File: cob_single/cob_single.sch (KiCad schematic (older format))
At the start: 26 parts, among them J1 Conn_01x03, J2 Conn_01x03, Q1 Q_NPN_BEC, Q2 Q_NPN_BEC, Q3 Q_NPN_BEC, U1 MOSFET_N_SI3424CDV-T1-GE3, U2 MOSFET_N_SI3424CDV-T1-GE3, U3 MOSFET_N_SI3424CDV-T1-GE3, U4 WS2811, U5 3_Inverter_TC7WH14FU,LJ(CT

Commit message: WIP rev v1.0
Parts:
- added H1, H2, H3, H4: MountingHole, homebrew:MountingHole_2.7mm_M2.5, symbol Mechanical:MountingHole
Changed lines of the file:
@@
 Wire Wire Line
 	1650 1150 1750 1150
+$Comp
+L Mechanical:MountingHole H1
+U 1 1 5DBB75AD
+P 9850 3250
+F 0 "H1" H 9950 3296 50  0000 L CNN
+F 1 "MountingHole" H 9950 3205 50  0000 L CNN
+F 2 "homebrew:MountingHole_2.7mm_M2.5" H 9850 3250 50  0001 C CNN
+F 3 "~" H 9850 3250 50  0001 C CNN
+	1    9850 3250
+	1    0    0    -1
+$EndComp
+$Comp
+L Mechanical:MountingHole H2
+U 1 1 5DBB979C
+P 9850 3400
+F 0 "H2" H 9950 3446 50  0000 L CNN
+F 1 "MountingHole" H 9950 3355 50  0000 L CNN
+F 2 "homebrew:MountingHole_2.7mm_M2.5" H 9850 3400 50  0001 C CNN
+F 3 "~" H 9850 3400 50  0001 C CNN
+	1    9850 3400
+	1    0    0    -1
+$EndComp
+$Comp
+L Mechanical:MountingHole H3
+U 1 1 5DBB99C6
+P 9850 3550
+F 0 "H3" H 9950 3596 50  0000 L CNN
+F 1 "MountingHole" H 9950 3505 50  0000 L CNN
+F 2 "homebrew:MountingHole_2.7mm_M2.5" H 9850 3550 50  0001 C CNN
+F 3 "~" H 9850 3550 50  0001 C CNN
+	1    9850 3550
+	1    0    0    -1
+$EndComp
+$Comp
+L Mechanical:MountingHole H4
+U 1 1 5DBB9B70
+P 9850 3700
+F 0 "H4" H 9950 3746 50  0000 L CNN
+F 1 "MountingHole" H 9950 3655 50  0000 L CNN
+F 2 "homebrew:MountingHole_2.7mm_M2.5" H 9850 3700 50  0001 C CNN
+F 3 "~" H 9850 3700 50  0001 C CNN
+	1    9850 3700
+	1    0    0    -1
+$EndComp
 $EndSCHEMATC

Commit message: Re-do revision 1.0 with 5V switching driver
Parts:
- removed Q1, Q2, Q3: Q_NPN_BEC, Package_TO_SOT_SMD:SOT-23, symbol Device:Q_NPN_BEC
- removed R6, R8: .36, Resistor_SMD:R_0805_2012Metric_Pad1.15x1.40mm_HandSolder, symbol Device:R
- removed R7: 100, Resistor_SMD:R_0603_1608Metric, symbol Device:R
- removed U1, U2, U3: MOSFET_N_SI3424CDV-T1-GE3, homebrew:6-TSOP-MOSFET-SI3424CDV-T1-GE3, symbol Homebrew:MOSFET_N_SI3424CDV-T1-GE3
- added C5, C6, C7, C8, C9: 10uF, Capacitor_SMD:C_0805_2012Metric, symbol Device:C
- added L1, L2, L3: 4.7uH, homebrew:1008_(2520_METRIC), symbol Device:L
- added U1, U2, U3: PAM2804_LED_DRIVER, Package_TO_SOT_SMD:TSOT-23-5, symbol Homebrew:PAM2804_LED_DRIVER
- R1, R4: value 100 -> .143
- R2: value .36 -> .143; footprint Resistor_SMD:R_0805_2012Metric_Pad1.15x1.40mm_HandSolder -> Resistor_SMD:R_0603_1608Metric
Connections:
- net labels added: B_LED_ANODE, B_LED_CATHODE, G_LED_ANODE, G_LED_CATHODE, R_LED_ANODE, R_LED_CATHODE
- net labels removed: B_LED, G_LED, R_LED
- wire segments 54 -> 59
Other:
- moved on the sheet: D1

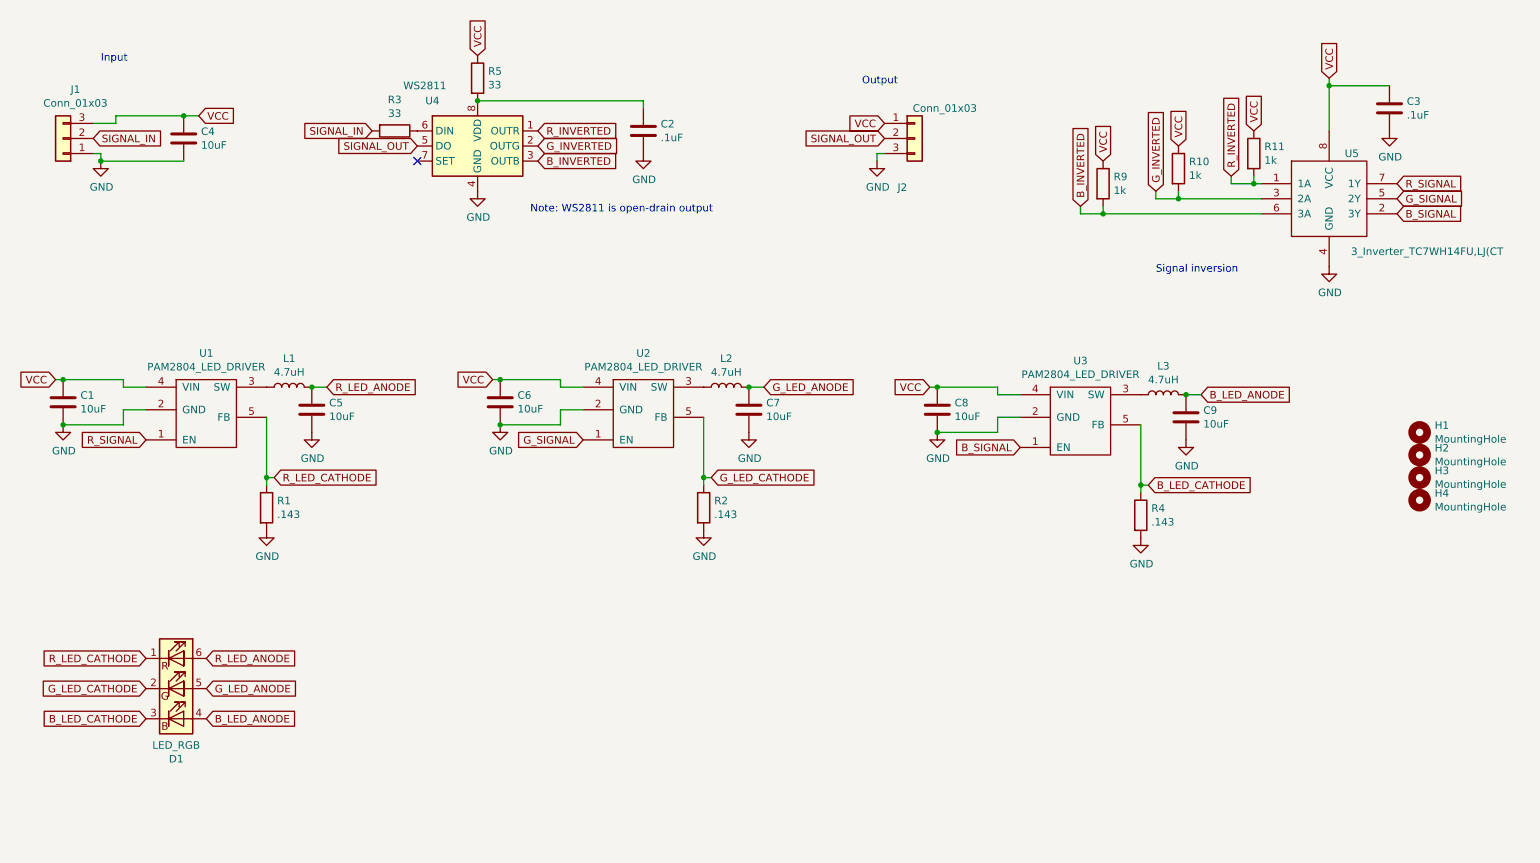
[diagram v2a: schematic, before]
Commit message: Convert v1.0 to 12v supply/12v tolerant switching driver.
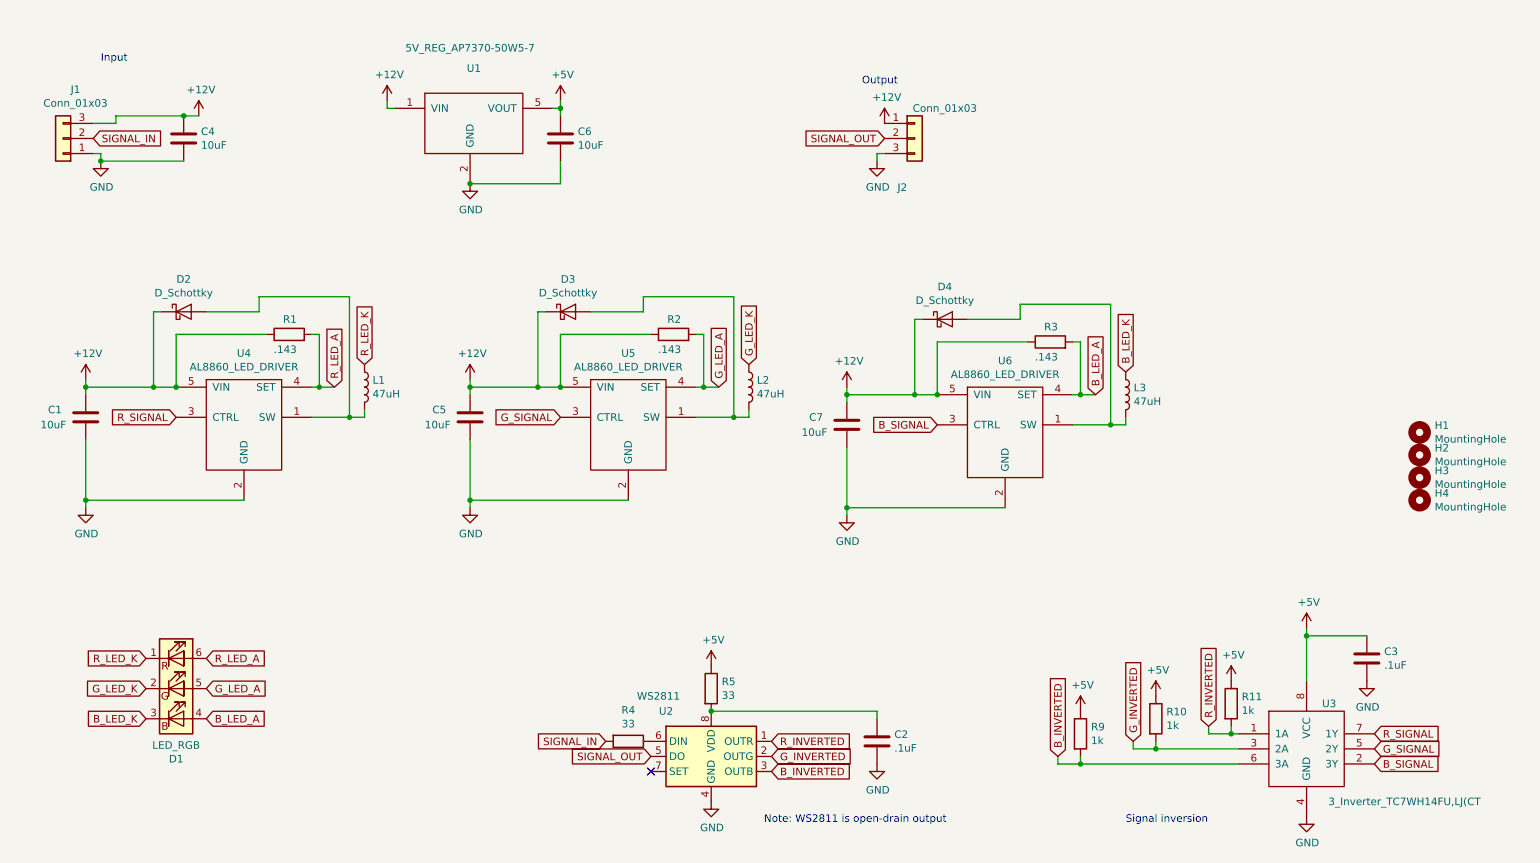
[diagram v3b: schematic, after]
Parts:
- removed C8, C9: 10uF, Capacitor_SMD:C_0805_2012Metric, symbol Device:C
- removed R4: .143, Resistor_SMD:R_0603_1608Metric, symbol Device:R
- removed U1, U2, U3: PAM2804_LED_DRIVER, Package_TO_SOT_SMD:TSOT-23-5, symbol Homebrew:PAM2804_LED_DRIVER
- added D2, D3, D4: D_Schottky, Diode_SMD:D_SOD-123F, symbol Device:D_Schottky
- added R3: .143, Resistor_SMD:R_0805_2012Metric, symbol Device:R
- added U1: 5V_REG_AP7370-50W5-7, Package_TO_SOT_SMD:TSOT-23-5, symbol Homebrew:5V_REG_AP7370-50W5-7
- added U4, U5, U6: AL8860_LED_DRIVER, homebrew:SOT-25, symbol Homebrew:AL8860_LED_DRIVER
- L1, L2, L3: value 4.7uH -> 47uH; footprint homebrew:1008_(2520_METRIC) -> Inductor_SMD:L_Taiyo-Yuden_NR-60xx
- R1, R2: footprint Resistor_SMD:R_0603_1608Metric -> Resistor_SMD:R_0805_2012Metric
- renumbered R3 to R4, U4 to U2, U5 to U3
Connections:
- net B_LED_CATHODE is gone; now on net B_LED_K: D1.3 (BK)
- net B_SIGNAL: now also U6.3 (CTRL)
- net GND: now also U1.2 (GND), U4.2 (GND), U5.2 (GND), U6.2 (GND); no longer R1.2, R2.2
- net G_SIGNAL: now also U5.3 (CTRL)
- net R_SIGNAL: now also U4.3 (CTRL)
- net R_LED_K: now reaches L1.1
- net R_LED_K: now also D1.1 (RK)
- net G_LED_K: now reaches L2.1
- net G_LED_K: now also D1.2 (GK)
- net B_LED_K: now reaches L3.1
- net B_LED_ANODE: no longer names the net of L3.2
- net B_LED_ANODE: now also D4.2 (A), U6.1 (SW); no longer D1.4 (BA)
- removed net G_LED_ANODE: C7.1, D1.5 (GA), L2.2
- net G_LED_CATHODE renamed +12V
- net +12V: now also C1.1, C4.1, C5.1, C7.1, J1.3 (Pin_3), J2.1 (Pin_1), R1.1, D2.1 (K), D3.1 (K), D4.1 (K), R3.1, U1.1 (VIN), U4.5 (VIN), U5.5 (VIN), U6.5 (VIN); no longer D1.2 (GK)
- removed net R_LED_ANODE: C5.1, D1.6 (RA), L1.2
- removed net R_LED_CATHODE: D1.1 (RK), R1.1
- net VCC renamed +5V
- net +5V: now also U1.5 (VOUT); no longer C1.1, C4.1, J1.3 (Pin_3), J2.1 (Pin_1)
- new net: D2.2 (A), L1.2, U4.1 (SW)
- new net: D3.2 (A), L2.2, U5.1 (SW)
- new net B_LED_A: D1.4 (BA), R3.2, U6.4 (SET)
- new net G_LED_A: D1.5 (GA), R2.2, U5.4 (SET)
- new net R_LED_A: D1.6 (RA), R1.2, U4.4 (SET)
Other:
- moved on the sheet: C1, C2, C3, R1, R10, R11, R4, R5, R9, U2, U3

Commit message: High-power revision 1.1:
- Fixed LED thermal pad to not connect to ground
- Fixed clearance for LED lens
- Added orientation for diodes and LED
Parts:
- removed D1: LED_RGB, LED_SMD:LED_RGB_Getian_GT-P6PRGB4303, symbol Device:LED_RGB
- added D1: LED_RGB_EP, homebrew:LED_RGB_EPISTAR_6PIN_RGB, symbol Device:LED_RGB_EP
- D2, D3, D4: footprint Diode_SMD:D_SOD-123F -> homebrew:D_SOD-123F
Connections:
- net B_LED_A: now also D1.4 (BA)
- net B_LED_K: now also D1.3 (BK)
- net G_LED_A: now also D1.5 (GA)
- net G_LED_K: now also D1.2 (GK)
- net R_LED_A: now also D1.6 (RA)
- net R_LED_K: now also D1.1 (RK)
- no-connect marks 1 -> 2
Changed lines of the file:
@@
 Text Notes 6150 950  0    50   ~ 0
 Output
-$Comp
-L Device:LED_RGB D1
-U 1 1 5DB6734D
-P 1600 4950
-F 0 "D1" H 1600 4483 50  0000 C CNN
-F 1 "LED_RGB" H 1600 4574 50  0000 C CNN
-F 2 "LED_SMD:LED_RGB_Getian_GT-P6PRGB4303" H 1600 4900 50  0001 C CNN
-F 3 "~" H 1600 4900 50  0001 C CNN
-	1    1600 4950
-	1    0    0    -1
-$EndComp
 Wire Wire Line
 	1200 1150 1650 1150
@@
 F 0 "D2" H 1650 2666 50  0000 C CNN
 F 1 "D_Schottky" H 1650 2575 50  0000 C CNN
-F 2 "Diode_SMD:D_SOD-123F" H 1650 2450 50  0001 C CNN
+F 2 "homebrew:D_SOD-123F" H 1650 2450 50  0001 C CNN
 F 3 "~" H 1650 2450 50  0001 C CNN
 	1    1650 2450
@@
 F 0 "D3" H 4200 2666 50  0000 C CNN
 F 1 "D_Schottky" H 4200 2575 50  0000 C CNN
-F 2 "Diode_SMD:D_SOD-123F" H 4200 2450 50  0001 C CNN
+F 2 "homebrew:D_SOD-123F" H 4200 2450 50  0001 C CNN
 F 3 "~" H 4200 2450 50  0001 C CNN
 	1    4200 2450
@@
 F 0 "D4" H 6700 2716 50  0000 C CNN
 F 1 "D_Schottky" H 6700 2625 50  0000 C CNN
-F 2 "Diode_SMD:D_SOD-123F" H 6700 2500 50  0001 C CNN
+F 2 "homebrew:D_SOD-123F" H 6700 2500 50  0001 C CNN
 F 3 "~" H 6700 2500 50  0001 C CNN
 	1    6700 2500
 	1    0    0    -1
 $EndComp
+$Comp
+L Device:LED_RGB_EP D1
+U 1 1 5DD2DD21
+P 1600 4950
+F 0 "D1" H 1600 5447 50  0000 C CNN
+F 1 "LED_RGB_EP" H 1600 5356 50  0000 C CNN
+F 2 "homebrew:LED_RGB_EPISTAR_6PIN_RGB" H 1600 4900 50  0001 C CNN
+F 3 "~" H 1600 4900 50  0001 C CNN
+	1    1600 4950
+	1    0    0    -1
+$EndComp
+NoConn ~ 1600 5450
 $EndSCHEMATC
